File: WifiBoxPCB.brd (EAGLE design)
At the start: 65 x 30 mm, 1 part, among them IC1 RTC72421

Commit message: Add files via upload
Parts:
- removed IC1: RTC72421, fox-electronics:DIL18
- added J1: 1140084168, 1140084168:1140084168
- added U1: MCP73871-2CCI/ML, MCP73871-2CCI_ML:QFN50P400X400X100-21N
- added U2: AZ1117EH-5.0TRG1, AZ1117EH-5.0TRG1:SOT230P700X180-4N
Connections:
- removed net VCC: IC1.16, IC1.17, IC1.18
- new net VSS: U1.10
- new net VSS_2: U1.11
- net GND: now also U2.1; no longer IC1.9
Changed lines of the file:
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@@
 <drawing>
 <settings>
-<setting alwaysvectorfont="yes"/>
+<setting alwaysvectorfont="no"/>
 <setting verticaltext="up"/>
 </settings>
@@
 <layer number="51" name="tDocu" color="7" fill="1" visible="yes" active="yes"/>
 <layer number="52" name="bDocu" color="7" fill="1" visible="yes" active="yes"/>
+<layer number="90" name="Modules" color="5" fill="1" visible="no" active="no"/>
 <layer number="91" name="Nets" color="2" fill="1" visible="no" active="no"/>
 <layer number="92" name="Busses" color="1" fill="1" visible="no" active="no"/>
@@
 </autorouter>
 <elements>
-<element name="IC1" library="fox-electronics" library_urn="urn:adsk.eagle:library:228" package="DIL18" package3d_urn="urn:adsk.eagle:package:13862/1" value="RTC72421" x="14" y="-5.5" smashed="yes">
-<attribute name="MF" value="" x="14" y="-5.5" size="1.778" layer="27" display="off"/>
-<attribute name="MPN" value="RTC72421B" x="14" y="-5.5" size="1.778" layer="27" display="off"/>
-<attribute name="NAME" x="2.316" y="-8.548" size="1.27" layer="25" ratio="10" rot="R90"/>
-<attribute name="OC_FARNELL" value="1216228" x="14" y="-5.5" size="1.778" layer="27" display="off"/>
-<attribute name="OC_NEWARK" value="01M8738" x="14" y="-5.5" size="1.778" layer="27" display="off"/>
-<attribute name="VALUE" x="4.475" y="-6.135" size="1.27" layer="27" ratio="10"/>
+<element name="J1" library="1140084168" package="1140084168" value="1140084168" x="-12.5" y="2" smashed="yes">
+<attribute name="AVAILABILITY" value="Unavailable" x="-12.5" y="2" size="1.778" layer="27" display="off"/>
+<attribute name="DESCRIPTION" value=" Conn; IC Socket; Micro SD; Right Angle; PCB Mount; MicroSD Ser. " x="-12.5" y="2" size="1.778" layer="27" display="off"/>
+<attribute name="MF" value="Amphenol" x="-12.5" y="2" size="1.778" layer="27" display="off"/>
+<attribute name="MP" value="1140084168" x="-12.5" y="2" size="1.778" layer="27" display="off"/>
+<attribute name="NAME" x="-7.28106875" y="-7.274090625" size="1.27078125" layer="25" align="center"/>
+<attribute name="PACKAGE" value="None" x="-12.5" y="2" size="1.778" layer="27" display="off"/>
+<attribute name="PRICE" value="None" x="-12.5" y="2" size="1.778" layer="27" display="off"/>
+</element>
+<element name="U1" library="MCP73871-2CCI_ML" package="QFN50P400X400X100-21N" value="MCP73871-2CCI/ML" x="-7" y="-17" smashed="yes">
+<attribute name="DESCRIPTION" value=" Fully Integrated Single Cell Lithium Ion/Lithium Polymer Charge Management Contr " x="-7" y="-17" size="1.778" layer="27" display="off"/>
+<attribute name="DIGI-KEY_PART_NUMBER" value="MCP73871-2CCI/ML-ND" x="-7" y="-17" size="1.778" layer="27" display="off"/>
+<attribute name="DIGI-KEY_PURCHASE_URL" value="https://www.digikey.com/product-detail/en/microchip-technology/MCP73871-2CCI-ML/MCP73871-2CCI-ML-ND/1680971?utm_source=snapeda&amp;utm_medium=aggregator&amp;utm_campaign=symbol" x="-7" y="-17" size="1.778" layer="27" display="off"/>
+<attribute name="MF" value="Microchip" x="-7" y="-17" size="1.778" layer="27" display="off"/>
+<attribute name="MP" value="MCP73871-2CCI/ML" x="-7" y="-17" size="1.778" layer="27" display="off"/>
+<attribute name="NAME" x="-11.677590625" y="-14.33071875" size="2.08458125" layer="25" ratio="10" rot="SR0"/>
+<attribute name="PACKAGE" value="QFN-20 Microchip" x="-7" y="-17" size="1.778" layer="27" display="off"/>
+<attribute name="VALUE" x="-12.82096875" y="-21.8042" size="2.084359375" layer="27" ratio="10" rot="SR0"/>
+</element>
+<element name="U2" library="AZ1117EH-5.0TRG1" package="SOT230P700X180-4N" value="AZ1117EH-5.0TRG1" x="-39" y="27" smashed="yes">
+<attribute name="AVAILABILITY" value="Unavailable" x="-39" y="27" size="1.778" layer="27" display="off"/>
+<attribute name="DESCRIPTION" value=" AZ1117E Series 5 V 1 A Fixed Surface Mount Voltage Regulator - SOT-223 " x="-39" y="27" size="1.778" layer="27" display="off"/>
+<attribute name="MF" value="Diodes Inc." x="-39" y="27" size="1.778" layer="27" display="off"/>
+<attribute name="MP" value="AZ1117EH-5.0TRG1" x="-39" y="27" size="1.778" layer="27" display="off"/>
+<attribute name="NAME" x="-66.1507" y="63.5604" size="9.0499" layer="25"/>
+<attribute name="PACKAGE" value="SOT-223 Diodes Inc." x="-39" y="27" size="1.778" layer="27" display="off"/>
+<attribute name="PRICE" value="None" x="-39" y="27" size="1.778" layer="27" display="off"/>
+<attribute name="VALUE" x="-66.4697" y="-19.149" size="9.15751875" layer="27"/>
 </element>
 </elements>
 <signals>
 <signal name="GND">
-<contactref element="IC1" pad="9"/>
+<contactref element="U2" pad="1"/>
 </signal>
-<signal name="VCC">
-<contactref element="IC1" pad="16"/>
-<contactref element="IC1" pad="17"/>
-<contactref element="IC1" pad="18"/>
-<wire x1="6.38" y1="-1.69" x2="8.92" y2="-1.69" width="0" layer="19" extent="1-1"/>
-<wire x1="3.84" y1="-1.69" x2="6.38" y2="-1.69" width="0" layer="19" extent="1-1"/>
+<signal name="VSS_2">
+<contactref element="U1" pad="11"/>
+</signal>
+<signal name="VSS">
+<contactref element="U1" pad="10"/>
 </signal>
 </signals>
@@
 </board>
 </drawing>
-<compatibility>
-<note version="8.2" severity="warning">
-Since Version 8.2, EAGLE supports online libraries. The ids
-of those online libraries will not be understood (or retained)
-with this version.
-</note>
-<note version="8.3" severity="warning">
-Since Version 8.3, EAGLE supports URNs for individual library
-assets (packages, symbols, and devices). The URNs of those assets
-will not be understood (or retained) with this version.
-</note>
-<note version="8.3" severity="warning">
-Since Version 8.3, EAGLE supports the association of 3D packages
-with devices in libraries, schematics, and board files. Those 3D
-packages will not be understood (or retained) with this version.
-</note>
-</compatibility>
 </eagle>

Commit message: testing move of J1#
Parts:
- moved J1 23.3 mm to (-18.5, 24.5)
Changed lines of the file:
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@@
 </autorouter>
 <elements>
-<element name="J1" library="1140084168" package="1140084168" value="1140084168" x="-12.5" y="2" smashed="yes">
-<attribute name="AVAILABILITY" value="Unavailable" x="-12.5" y="2" size="1.778" layer="27" display="off"/>
-<attribute name="DESCRIPTION" value=" Conn; IC Socket; Micro SD; Right Angle; PCB Mount; MicroSD Ser. " x="-12.5" y="2" size="1.778" layer="27" display="off"/>
-<attribute name="MF" value="Amphenol" x="-12.5" y="2" size="1.778" layer="27" display="off"/>
-<attribute name="MP" value="1140084168" x="-12.5" y="2" size="1.778" layer="27" display="off"/>
-<attribute name="NAME" x="-7.28106875" y="-7.274090625" size="1.27078125" layer="25" align="center"/>
-<attribute name="PACKAGE" value="None" x="-12.5" y="2" size="1.778" layer="27" display="off"/>
-<attribute name="PRICE" value="None" x="-12.5" y="2" size="1.778" layer="27" display="off"/>
+<element name="J1" library="1140084168" package="1140084168" value="1140084168" x="-18.5" y="24.5" smashed="yes">
+<attribute name="AVAILABILITY" value="Unavailable" x="-18.5" y="24.5" size="1.778" layer="27" display="off"/>
+<attribute name="DESCRIPTION" value=" Conn; IC Socket; Micro SD; Right Angle; PCB Mount; MicroSD Ser. " x="-18.5" y="24.5" size="1.778" layer="27" display="off"/>
+<attribute name="MF" value="Amphenol" x="-18.5" y="24.5" size="1.778" layer="27" display="off"/>
+<attribute name="MP" value="1140084168" x="-18.5" y="24.5" size="1.778" layer="27" display="off"/>
+<attribute name="NAME" x="-13.28106875" y="15.225909375" size="1.27078125" layer="25" align="center"/>
+<attribute name="PACKAGE" value="None" x="-18.5" y="24.5" size="1.778" layer="27" display="off"/>
+<attribute name="PRICE" value="None" x="-18.5" y="24.5" size="1.778" layer="27" display="off"/>
 </element>
 <element name="U1" library="MCP73871-2CCI_ML" package="QFN50P400X400X100-21N" value="MCP73871-2CCI/ML" x="-7" y="-17" smashed="yes">

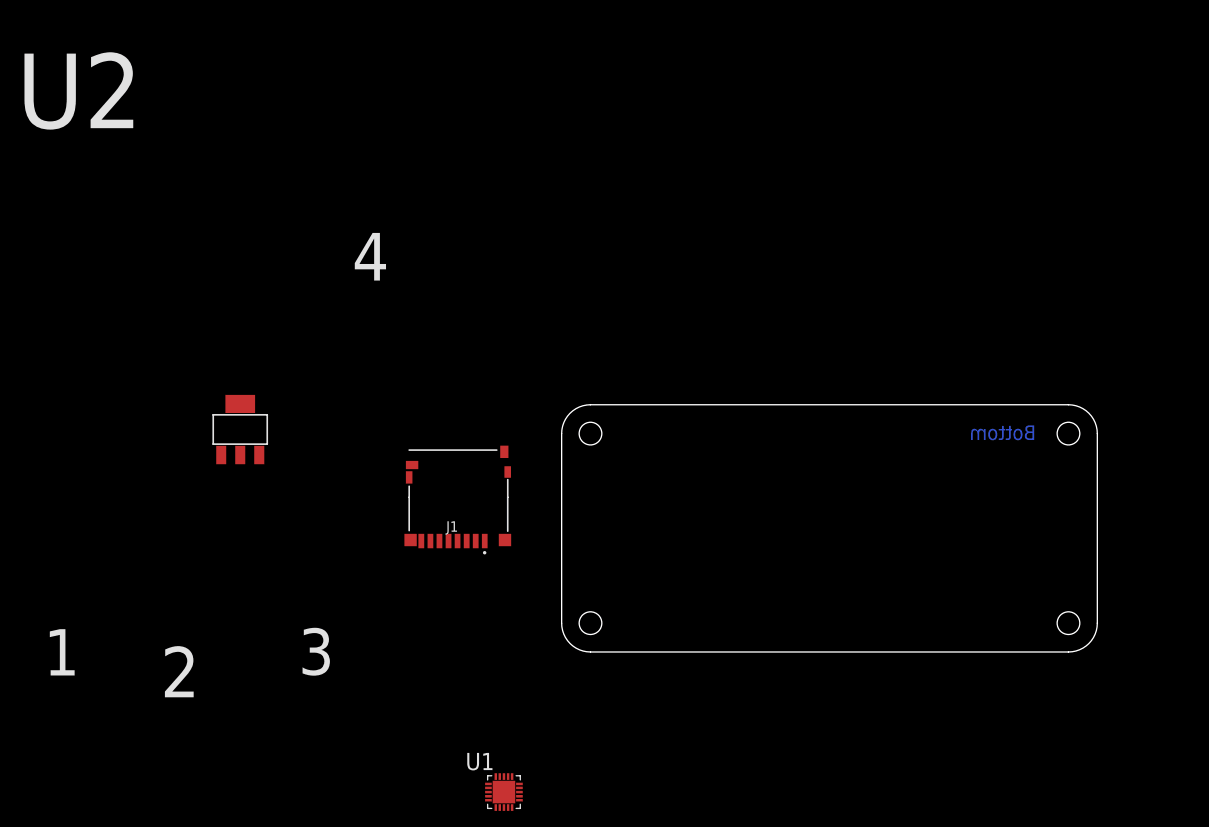
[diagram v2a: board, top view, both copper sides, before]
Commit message: reset board and schematic down to just the micro SD
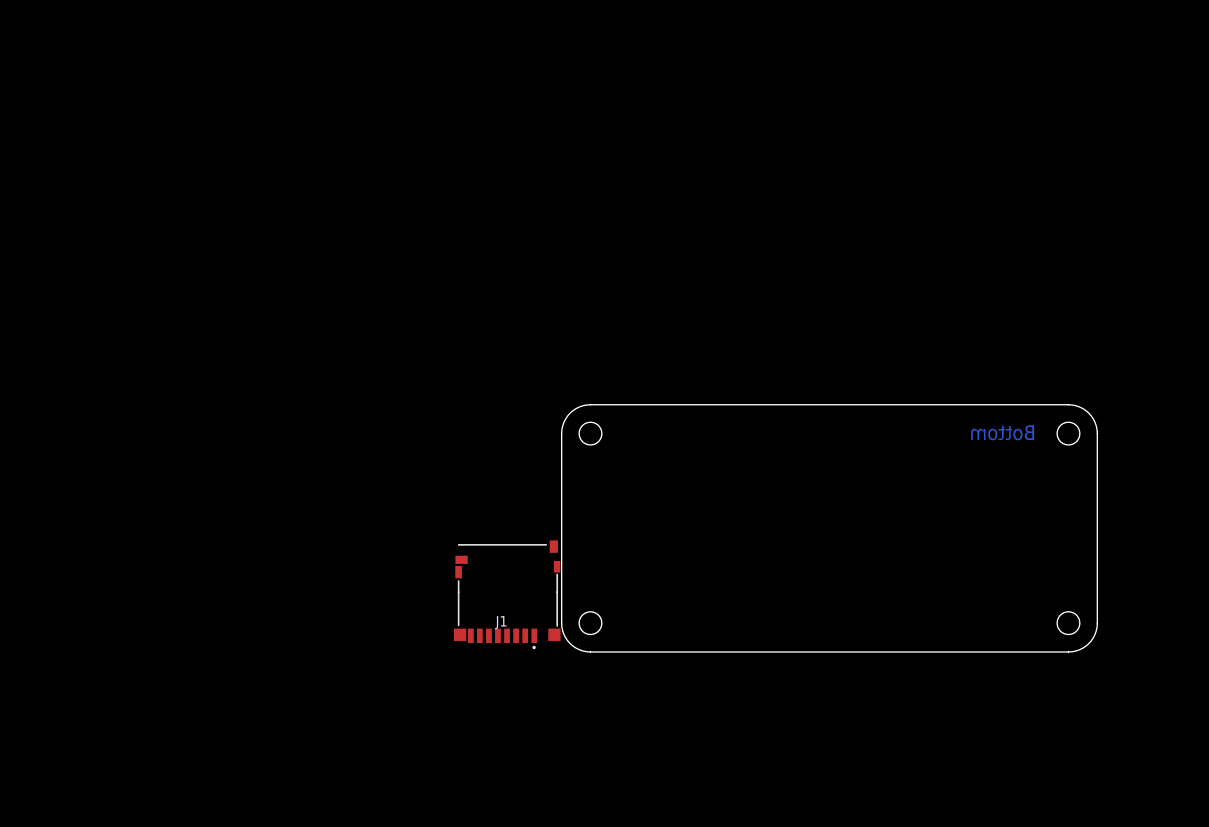
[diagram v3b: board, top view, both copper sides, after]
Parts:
- removed U1: MCP73871-2CCI/ML, MCP73871-2CCI_ML:QFN50P400X400X100-21N
- removed U2: AZ1117EH-5.0TRG1, AZ1117EH-5.0TRG1:SOT230P700X180-4N
- moved J1 13.0 mm to (-12.5, 13.0)
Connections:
- removed net GND: U2.1
- removed net VSS: U1.10
- removed net VSS_2: U1.11
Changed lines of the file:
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@@
 <layer number="51" name="tDocu" color="7" fill="1" visible="yes" active="yes"/>
 <layer number="52" name="bDocu" color="7" fill="1" visible="yes" active="yes"/>
+<layer number="88" name="SimResults" color="9" fill="1" visible="no" active="no"/>
+<layer number="89" name="SimProbes" color="9" fill="1" visible="no" active="no"/>
 <layer number="90" name="Modules" color="5" fill="1" visible="no" active="no"/>
 <layer number="91" name="Nets" color="2" fill="1" visible="no" active="no"/>
@@
 </autorouter>
 <elements>
-<element name="J1" library="1140084168" package="1140084168" value="1140084168" x="-18.5" y="24.5" smashed="yes">
-<attribute name="AVAILABILITY" value="Unavailable" x="-18.5" y="24.5" size="1.778" layer="27" display="off"/>
-<attribute name="DESCRIPTION" value=" Conn; IC Socket; Micro SD; Right Angle; PCB Mount; MicroSD Ser. " x="-18.5" y="24.5" size="1.778" layer="27" display="off"/>
-<attribute name="MF" value="Amphenol" x="-18.5" y="24.5" size="1.778" layer="27" display="off"/>
-<attribute name="MP" value="1140084168" x="-18.5" y="24.5" size="1.778" layer="27" display="off"/>
-<attribute name="NAME" x="-13.28106875" y="15.225909375" size="1.27078125" layer="25" align="center"/>
-<attribute name="PACKAGE" value="None" x="-18.5" y="24.5" size="1.778" layer="27" display="off"/>
-<attribute name="PRICE" value="None" x="-18.5" y="24.5" size="1.778" layer="27" display="off"/>
-</element>
-<element name="U1" library="MCP73871-2CCI_ML" package="QFN50P400X400X100-21N" value="MCP73871-2CCI/ML" x="-7" y="-17" smashed="yes">
-<attribute name="DESCRIPTION" value=" Fully Integrated Single Cell Lithium Ion/Lithium Polymer Charge Management Contr " x="-7" y="-17" size="1.778" layer="27" display="off"/>
-<attribute name="DIGI-KEY_PART_NUMBER" value="MCP73871-2CCI/ML-ND" x="-7" y="-17" size="1.778" layer="27" display="off"/>
-<attribute name="DIGI-KEY_PURCHASE_URL" value="https://www.digikey.com/product-detail/en/microchip-technology/MCP73871-2CCI-ML/MCP73871-2CCI-ML-ND/1680971?utm_source=snapeda&amp;utm_medium=aggregator&amp;utm_campaign=symbol" x="-7" y="-17" size="1.778" layer="27" display="off"/>
-<attribute name="MF" value="Microchip" x="-7" y="-17" size="1.778" layer="27" display="off"/>
-<attribute name="MP" value="MCP73871-2CCI/ML" x="-7" y="-17" size="1.778" layer="27" display="off"/>
-<attribute name="NAME" x="-11.677590625" y="-14.33071875" size="2.08458125" layer="25" ratio="10" rot="SR0"/>
-<attribute name="PACKAGE" value="QFN-20 Microchip" x="-7" y="-17" size="1.778" layer="27" display="off"/>
-<attribute name="VALUE" x="-12.82096875" y="-21.8042" size="2.084359375" layer="27" ratio="10" rot="SR0"/>
-</element>
-<element name="U2" library="AZ1117EH-5.0TRG1" package="SOT230P700X180-4N" value="AZ1117EH-5.0TRG1" x="-39" y="27" smashed="yes">
-<attribute name="AVAILABILITY" value="Unavailable" x="-39" y="27" size="1.778" layer="27" display="off"/>
-<attribute name="DESCRIPTION" value=" AZ1117E Series 5 V 1 A Fixed Surface Mount Voltage Regulator - SOT-223 " x="-39" y="27" size="1.778" layer="27" display="off"/>
-<attribute name="MF" value="Diodes Inc." x="-39" y="27" size="1.778" layer="27" display="off"/>
-<attribute name="MP" value="AZ1117EH-5.0TRG1" x="-39" y="27" size="1.778" layer="27" display="off"/>
-<attribute name="NAME" x="-66.1507" y="63.5604" size="9.0499" layer="25"/>
-<attribute name="PACKAGE" value="SOT-223 Diodes Inc." x="-39" y="27" size="1.778" layer="27" display="off"/>
-<attribute name="PRICE" value="None" x="-39" y="27" size="1.778" layer="27" display="off"/>
-<attribute name="VALUE" x="-66.4697" y="-19.149" size="9.15751875" layer="27"/>
+<element name="J1" library="1140084168" package="1140084168" value="1140084168" x="-12.5" y="13" smashed="yes">
+<attribute name="AVAILABILITY" value="Unavailable" x="-12.5" y="13" size="1.778" layer="27" display="off"/>
+<attribute name="DESCRIPTION" value=" Conn; IC Socket; Micro SD; Right Angle; PCB Mount; MicroSD Ser. " x="-12.5" y="13" size="1.778" layer="27" display="off"/>
+<attribute name="MF" value="Amphenol" x="-12.5" y="13" size="1.778" layer="27" display="off"/>
+<attribute name="MP" value="1140084168" x="-12.5" y="13" size="1.778" layer="27" display="off"/>
+<attribute name="NAME" x="-7.28106875" y="3.725909375" size="1.27078125" layer="25" align="center"/>
+<attribute name="PACKAGE" value="None" x="-12.5" y="13" size="1.778" layer="27" display="off"/>
+<attribute name="PRICE" value="None" x="-12.5" y="13" size="1.778" layer="27" display="off"/>
 </element>
 </elements>
 <signals>
-<signal name="GND">
-<contactref element="U2" pad="1"/>
-</signal>
-<signal name="VSS_2">
-<contactref element="U1" pad="11"/>
-</signal>
-<signal name="VSS">
-<contactref element="U1" pad="10"/>
-</signal>
 </signals>
 <mfgpreviewcolors>

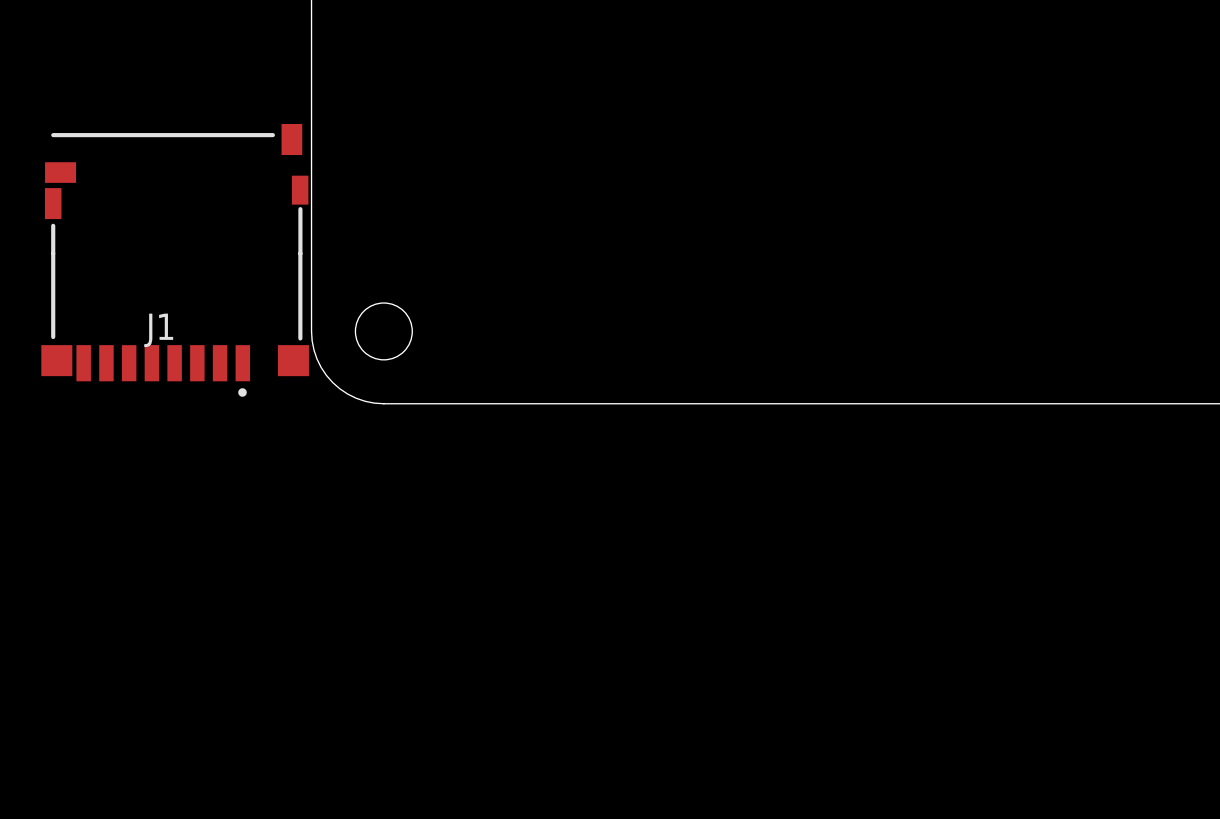
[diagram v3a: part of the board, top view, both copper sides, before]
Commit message: Add frame, +5V, +3.3V, GND, 2x20 connector customized for Raspberry Pi, customized MicroSD devices to library, change Schematic to use parts from ConnectBox Library, start to wire MicroSD socket to Pi 40 pin connector.
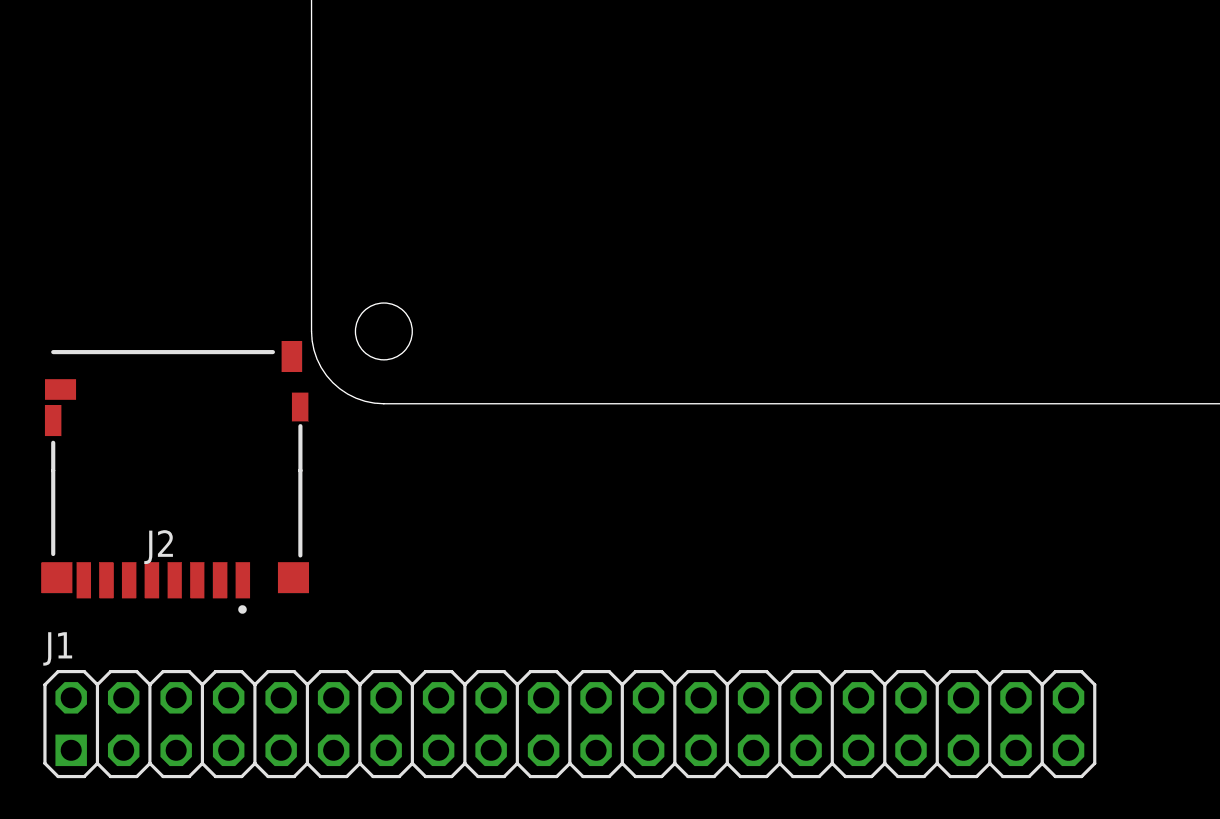
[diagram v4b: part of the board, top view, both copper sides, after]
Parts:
- added J2: 1140084168_1140084168, ConnectBox_2019:1140084168_1140084168
- J1: value 1140084168 -> CONNECTOR_PI_40_PIN; device 1140084168:1140084168 -> ConnectBox_2019:2X20
- moved J1 37.9 mm to (12.5, -15.5)
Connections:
- new net +3V3: J1.1, J2.4
- new net CS: J1.24, J2.2
- new net GND: J1.39, J2.6
- new net MOSI: J1.19, J2.3
